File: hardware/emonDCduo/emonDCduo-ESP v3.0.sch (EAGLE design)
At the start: 84 parts, among them IC1 ACS758LCB-050B-PFF-T, IC2 ACS758LCB-050B-PFF-T, IC3 LM358D, P1 B4B-PH-K, Y1 32Khz

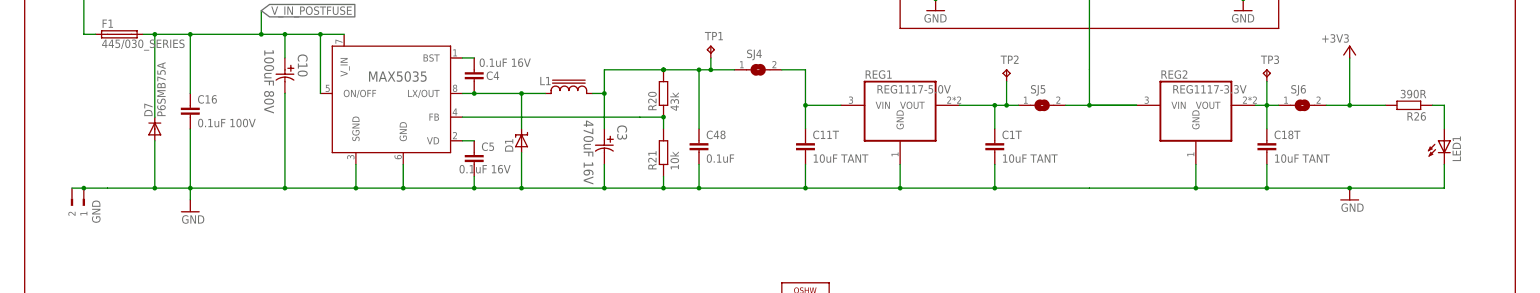
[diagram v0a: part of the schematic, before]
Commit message: starting v3.0 and ASC770 breakout
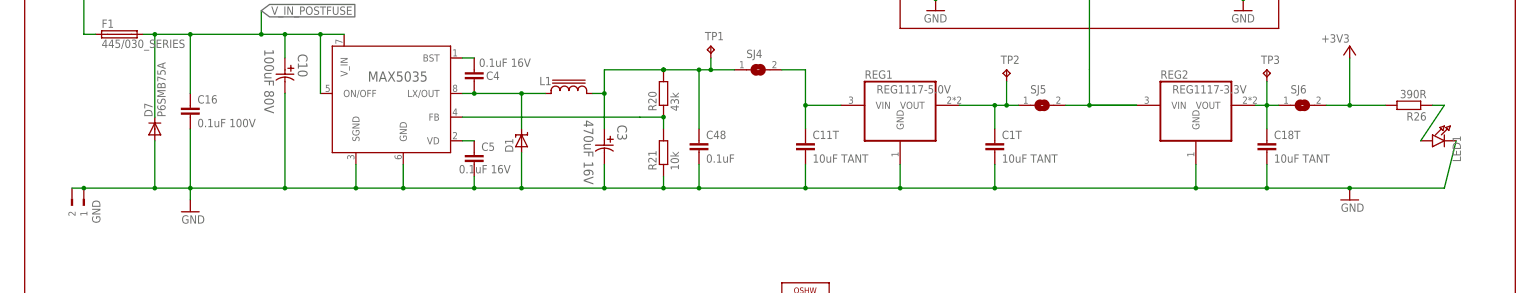
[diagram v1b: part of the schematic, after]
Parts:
- LED1: device led:LEDCHIP-LED0805 -> microbuilder:LED1206
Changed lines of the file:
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@@
 <part name="F1" library="LITTELFUSE 455:030 SERIES" deviceset="445/030_SERIES" device=""/>
 <part name="R26" library="rcl" library_urn="urn:adsk.eagle:library:334" deviceset="R-EU_" device="R0603" package3d_urn="urn:adsk.eagle:package:23555/2" value="390R"/>
-<part name="LED1" library="led" library_urn="urn:adsk.eagle:library:259" deviceset="LED" device="CHIP-LED0805" package3d_urn="urn:adsk.eagle:package:15818/2"/>
+<part name="LED1" library="microbuilder" deviceset="LED" device="1206"/>
 <part name="SJ2" library="jumper-con_db" deviceset="SJ-CON" device="CON"/>
 <part name="SJ3" library="jumper-con_db" deviceset="SJ-CON" device="CON"/>
@@
 <wire x1="30.48" y1="226.06" x2="50.8" y2="226.06" width="0.1524" layer="91"/>
 <wire x1="50.8" y1="226.06" x2="71.12" y2="226.06" width="0.1524" layer="91"/>
-<wire x1="71.12" y1="226.06" x2="91.44" y2="226.06" width="0.1524" layer="91"/>
-<wire x1="91.44" y1="226.06" x2="114.3" y2="226.06" width="0.1524" layer="91"/>
+<wire x1="71.12" y1="226.06" x2="114.3" y2="226.06" width="0.1524" layer="91"/>
 <wire x1="129.54" y1="226.06" x2="114.3" y2="226.06" width="0.1524" layer="91"/>
 <junction x="129.54" y="226.06"/>
@@
 <wire x1="-101.6" y1="226.06" x2="-109.22" y2="226.06" width="0.1524" layer="91"/>
 <pinref part="GND" gate="G$1" pin="1"/>
-<wire x1="-109.22" y1="226.06" x2="-119.38" y2="226.06" width="0.1524" layer="91"/>
-<wire x1="-119.38" y1="226.06" x2="-124.46" y2="226.06" width="0.1524" layer="91"/>
+<wire x1="-109.22" y1="226.06" x2="-124.46" y2="226.06" width="0.1524" layer="91"/>
 <wire x1="-124.46" y1="226.06" x2="-127" y2="226.06" width="0.1524" layer="91"/>
 <junction x="-124.46" y="226.06"/>
 <pinref part="GND" gate="G$1" pin="2"/>
 <pinref part="LED1" gate="G$1" pin="C"/>
-<wire x1="167.64" y1="231.14" x2="167.64" y2="226.06" width="0.1524" layer="91"/>
+<wire x1="170.18" y1="236.22" x2="167.64" y2="226.06" width="0.1524" layer="91"/>
 <wire x1="167.64" y1="226.06" x2="147.32" y2="226.06" width="0.1524" layer="91"/>
 <wire x1="-12.7" y1="226.06" x2="0" y2="226.06" width="0.1524" layer="91"/>
@@
 <pinref part="LED1" gate="G$1" pin="A"/>
 <wire x1="165.1" y1="243.84" x2="167.64" y2="243.84" width="0.1524" layer="91"/>
-<wire x1="167.64" y1="243.84" x2="167.64" y2="238.76" width="0.1524" layer="91"/>
-</segment>
-</net>
+<wire x1="167.64" y1="243.84" x2="162.56" y2="236.22" width="0.1524" layer="91"/>
+</segment>
+</net>

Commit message: commit v3.0
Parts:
- removed C10: 100uF 80V, Panasonic-EEE-EEV-EEF-ECQ:EEV-FK1K101Q-CASE-H13
- removed C16: 0.1uF 100V, rcl:C-EUC0603
- removed C2: 100nF, rcl:C-EUC0603
- removed C3: 470uF 16V, Panasonic-EEEFK_EEEFP:EEE-FK1C471P-CASE-F
- removed C4, C5: 0.1uF 16V, rcl:C-EUC0603
- removed C48, C7, C9: 0.1uF, rcl:C-EUC0603
- removed D1: MBRS1100T3G, diodes:MBRS1100T3G
- removed IC1, IC2: ACS758LCB-050B-PFF-T, allegro:ACS758LCB-050B-PFF-T
- removed IC3: LM358D, linear:LM358D
- removed J1: (no value), SparkFun-Connectors:CONN_02
- removed L1: SRR1208, inductor-bourns:SRR1208
- removed R11: 5.23k, rcl:R-EU_0204/7
- removed R20: 43k, rcl@1:R-EU_R0603
- removed R21: 10k, rcl@1:R-EU_R0603
- removed REG0: MAX5035, MAX5035:MAX5035
- removed SJ7: (no value), jumper:SJ
- removed UART_RFM: UART_RFM, JeeLabs:MA06-1
- added 7.62_BARRIER: GMSTBA2, con-phoenix-762:GMSTBA2
- added C12, C13, C14, C15, C17, C18, C20: 1nF, rcl:C-EUC0603
- added C19: 0.1uF, rcl:C-EUC0603
- added C23, C24, C25: 0.1uF 100V, rcl:C-EUC0603
- added D2, D3, D4, D5: P6SMB75A, diode:DIODE-DO214AA
- added EBW_A, EBW_B: EBW_SERIES_15.2MM, EBW series SHUNT:EBW_SERIES_15.2MM
- added F2, F3, F4, F5: (no value), fuse:TR5
- added LM258: (no value), microbuilder:LM358
- added MCP3208: MCP3208-BI/SL, MCP3208:MCP3208-BI/SL
- added MOUNT_10.16_A, MOUNT_10.16_B: MOLEX_39970-003, 10.16mm terminal block:MOLEX_39970-003
- added MOUNT_7.62_A, MOUNT_7.62_B: GMSTBV2, con-phoenix-762:GMSTBV2
- added PWR, REF_SEL_A, REF_SEL_B: 455-1750-1-ND, SparkFun-Connectors:CONN_03
- added R4: 1K, rcl:R-EU_R0603
- added R8: 2K, rcl:R-EU_R0603
- added SHUNTMON-A, SHUNTMON-B: LMP8481, lmp8481b:LMP8481-H
- added SJ1: (no value), jumper-con_db:SJ-CONCON
- added TP4, TP5, TP6, TP7: TPPAD1-13Y, testpad:TPPAD1-13Y
- C11: value 0.1uF 100V -> 1nF; MPN C1608X7S2A104K080AB -> (none)
- C11T, C18T, C1T: device rcl:C-EUC0603 -> rcl7:CPOL-EUC0603POL
- C7T: device rcl@1:C-EUC0603 -> rcl7:CPOL-EUC0603POL
- R1, R14: value 1.5M 3.5kV -> 1M 100V; device rcl7:R-EU_0411/15 -> rcl:R-EU_R0603
- R10: value 16.56k -> 174R; device rcl:R-EU_0204/7 -> rcl7:R-EU_0207/10
- R13: value 5.23k -> 10k; device rcl7:R-EU_R0603 -> rcl7:R-EU_0207/10
- R15, R2: value 100K -> 56K
- R26: value 390R -> 174R
- R5: value 517.77k -> 5.6k; device rcl7:R-EU_R0603 -> rcl7:R-EU_0207/10
- renumbered BOOT to ESPBOOT
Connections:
- net N$30 renamed RESET
- removed net BST: C4.1, REG0.BST
- removed net CH6: J5.2
- removed net LX: C4.2, D1.C, L1.1, REG0.LX/OUT
- removed net N$10: C7T.1, PCF8523.VDD, R9.1
- removed net N$20: UART_RFM.5
- removed net N$3: IC2.IP+, MH4.MOUNT
- removed net N$301: C2.2, UART_RFM.1
- removed net N$4: J1.2
- removed net N$6: J1.1
- removed net N$9: IC3B.+IN, R1.1, R2.2
- removed net PRE_6.5V: C3.1, C48.1, L1.2, R20.2, SJ4.1, TP1.TP
- removed net VD: C5.1, REG0.VD
- new net GPIO12A: MCP3208.DOUT, R4.1
- new net LOAD-NEG-A_T: C1.1, C23.2, D2.C, F2.2, SHUNTMON-A.RSN
- new net LOAD-NEG-B: EBW_A.P$2, F4.1, MH4.MOUNT, MOUNT_10.16_B.P$1, MOUNT_7.62_A-2.1
- new net LOAD-NEG-B_T: C24.2, C8.1, D4.C, F4.2, SHUNTMON-B.RSN
- new net REF_A_INPUT: REF_SEL_A.2, SHUNTMON-A.REFA, SHUNTMON-A.REFB
- new net REF_B_INPUT: REF_SEL_B.2, SHUNTMON-B.REFA, SHUNTMON-B.REFB
- new net SOURCE-POS-A_T: C1.2, C25.1, D3.C, F3.2, R14.2, SHUNTMON-A.RSP
- new net SOURCE-POS-B_T: C6.1, C8.2, D5.C, F5.2, R1.2, SHUNTMON-B.RSP
- new net VDD_PCF: C7T.+, PCF8523.VDD, R9.1
- new net VSENSE_B: LM258G$2.+IN, R1.1, R2.2
- net +3V3: now also C18.1, MCP3208.CH6
- net +5V: now also C19.1, LM258G$1.V+, MCP3208.VDD, MCP3208.VREF, R13.2, SHUNTMON-A.VCC, SHUNTMON-B.VCC; no longer C1.1, C8.1, IC1.VCC, IC2.VCC, R10.2, R5.1, UART_RFM.4
- net 3.3V_PRE: now also C18T.+; no longer C18T.1
- net 5V_PRE: now also 7.62_BARRIER-2.1, C1T.+; no longer C1T.1
- net 6.5V: now also C11T.+; no longer C11T.1
- net ADCSHUNT_A: now also C17.1, MCP3208.CH0, SHUNTMON-A.VOUT; no longer C6.1, IC1.VOUT
- net ADCSHUNT_B: now also C12.1, MCP3208.CH2, SHUNTMON-B.VOUT; no longer C11.1, IC2.VOUT
- net BI_REF: now also C14.1, MCP3208.CH4, R13.1, R5.2, REF_SEL_A.3, REF_SEL_B.3; no longer C7.1, R10.1, R11.2
- net CH7: now also C20.1, MCP3208.CH7
- net D0/RX: no longer UART_RFM.2
- net D1/TX: no longer UART_RFM.3
- net GND: now also 7.62_BARRIER-1.1, C11T.-, C18T.-, C19.2, C1T.-, C23.1, C24.1, C25.2, C7T.-, D2.A, D3.A, D4.A, D5.A, J5.2, LM258G$1.V-, MCP3208.AGND, MCP3208.DGND, R10.1, R8.2, SHUNTMON-A.GND, SHUNTMON-B.GND, TP6.TP, TP7.TP; no longer C1.2, C10.2, C11.2, C11T.2, C16.2, C18T.2, C1T.2, C3.2, C48.2, C5.2, C7.2, C7T.2, C8.2, C9.2, D1.A, IC1.GND, IC2.GND, R11.1, R13.2, R21.1, REG0.GND, REG0.SGND, UART_RFM.6
- net GPIO12: now also R4.2, R8.1
- net GPIO13: now also MCP3208.DIN
- net GPIO14: now also MCP3208.CLK
- net GPIO16: now also SJ1.2; no longer SJ7.1
- net GPIO2: now also MCP3208.!CS
- net LOAD-NEG-A: now also EBW_B.P$2, F2.1, MOUNT_10.16_A.P$1, MOUNT_7.62_B-2.1; no longer IC1.IP+
- net N$1: now also SJ4.1, TP1.TP, TP5.TP; no longer R20.1, R21.2, REG0.FB
- net RST: now also SJ1.1; no longer SJ7.2
- net SOURCE-POS-A: now also EBW_B.P$1, F3.1, MOUNT_10.16_A.P$2, MOUNT_7.62_B-1.1, PWR.3; no longer IC1.IP-, R14.2
- net SOURCE-POS-B: now also EBW_A.P$1, F5.1, MOUNT_10.16_B.P$2, MOUNT_7.62_A-1.1, PWR.1; no longer IC2.IP-, R1.2
- net UNI_REF: now also C15.1, MCP3208.CH5, R10.2, R5.1, REF_SEL_A.1, REF_SEL_B.1; no longer C9.1, R13.1, R5.2
- net VSENSE_A: now also LM258G$1.+IN; no longer IC3A.+IN
- net VSENSE_A_BUFF: now also C11.1, LM258G$1.-IN, LM258G$1.OUT, MCP3208.CH1; no longer IC3A.-IN, IC3A.OUT
- net VSENSE_B_BUFF: now also C13.1, LM258G$2.-IN, LM258G$2.OUT, MCP3208.CH3; no longer IC3B.-IN, IC3B.OUT
- net V_IN_POSTFUSE: now also TP4.TP; no longer C10.1, C16.1, REG0.ON/OFF, REG0.V_IN
- net V_IN_PREFUSE: now also PWR.2
- net _RESET: no longer C2.1
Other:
- note added: "50mV MIN output desirable"
- note added: "MCP3208"
- note added: "SPI LCD DISPLAY"
- note added: "designed by Daniel Bates November 2018"
- note added: "emonDC v3.0 use of ESP module inspired by Heatpumpmonitor project. RTC layout taken from IoTaWatt."
- note removed: "I2C LCD DISPLAY"
- note removed: "STM32"
- note removed: "designed by Daniel Bates July 2018"
- note removed: "emonDC v2.4 based on emonTx and Heatpumpmonitor"
- moved on the sheet: C1, C11, C6, C8, J5, LED1, MH1, MH2, MH3, MH4, R10, R13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

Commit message: commit v3.1
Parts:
- removed C21, C22: 100nF, rcl:C-EUC0603
- removed C23, C24: 0.1uF 100V, rcl:C-EUC0603
- removed MOUNT_7.62_A, MOUNT_7.62_B: GMSTBV2, con-phoenix-762:GMSTBV2
- removed R18: 2k, rcl:R-EU_R0603
- removed R26: 174R, rcl:R-EU_R0603
- removed R27, R28: 10K, rcl:R-EU_R0603
- removed SJ3: (no value), jumper-con_db:SJ-CONCON
- added C10, C9: 1nF, rcl:C-EUC0603
- added C2, C4, C5, C7: 0.1uF 100V, rcl:C-EUC0603
- added R11, R20, R21: 10K, rcl:R-EU_R0603
- added R22: 1K, rcl@1:R-EU_R0603
- added TP10, TP11, TP8, TP9: TPPAD1-13Y, testpad:TPPAD1-13Y
- C17, C18: value 1nF -> 0.1uF
- C33T: value 10uF -> 10uF TANT
- LED1: value (none) -> PWR_ON
- R10: value 174R -> 2K; device rcl7:R-EU_0207/10 -> rcl:R-EU_R0603; MPN (none) -> MCWR06X5901FTL
- R13: value 10k -> 10K; device rcl7:R-EU_0207/10 -> rcl:R-EU_R0603
- R14: value 1M 100V -> 1k; MPN MCWR06X1003FTL -> (none)
- R15: value 56K -> 2k; MPN MCWR06X5901FTL -> (none)
- R17: value 1k -> 10K
- R3: value 10K -> 1M 100V; MPN (none) -> MCWR06X1003FTL
- R4: value 1K -> 56K
- R5: value 5.6k -> 174R; device rcl7:R-EU_0207/10 -> rcl:R-EU_R0603
- R6: value 10K -> 10k; device rcl:R-EU_R0603 -> rcl7:R-EU_0207/10
- R7: value 10K -> 5.6k; device rcl:R-EU_R0603 -> rcl7:R-EU_0207/10
- R8: value 2K -> 174R; device rcl:R-EU_R0603 -> rcl7:R-EU_0207/10; MPN MCWR06X5901FTL -> (none)
- R9: device rcl@1:R-EU_R0603 -> rcl:R-EU_R0603; MPN (none) -> MCWR06X5901FTL
- SJ2: device jumper-con_db:SJ-CONCON -> jumper:SJ
- UART: value UART_ESP -> UART
- renumbered C11T to C30T, C18T to C32T, C1T to C31T, C20 to C16, C25 to C3, C7T to C33T, D7 to D1, R19 to R16, UART_ESP to UART
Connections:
- removed net N$24: R9.2, SJ2.2
- removed net VCC_ESP: C22.2, ESP-12.VCC, R12.2, R16.2, R6.2, R7.2, SJ3.1
- new net VDD_RTC_POSTJUMPER: R20.1, R21.1, R22.2, SJ2.2
- net +3V3: now also C15.1, C17.2, ESP-12.VCC, R12.2, R13.2, R16.2, R17.2, R5.2; no longer C18.1, R26.2, R27.1, R28.1, SJ3.2
- net +5V: now also R6.2; no longer R13.2
- net ADCSHUNT_A: now also C9.1; no longer C17.1
- net ADCSHUNT_B: now also C11.1; no longer C12.1
- net BI_REF: now also C13.1, R6.1, R7.2; no longer C14.1, R13.1, R5.2
- net CH_PD: now also C18.1, R17.1; no longer C21.1, R7.1
- net ESPRX: now also R14.2, R15.1; no longer R17.2, R18.1
- net GND: now also C1.2, C17.1, C4.2, C7.2, C8.2, R10.2, R11.2, R15.2, R4.1, R8.1; no longer C22.1, C23.1, C24.1, R10.1, R15.1, R18.2, R3.2, R8.2
- net GPIO0: now also R13.1; no longer R12.1
- net GPIO12: now also R10.1, R9.2; no longer R4.2, R8.1
- net GPIO12A: now also R9.1; no longer R4.1
- net GPIO15: now also R11.1; no longer R3.1
- net GPIO2: now also R12.1; no longer R6.1
- net LOAD-NEG-A: now also TP11.TP; no longer MOUNT_7.62_B-2.1
- net LOAD-NEG-A_T: now also C2.1; no longer C23.2
- net LOAD-NEG-B: now also TP9.TP; no longer MOUNT_7.62_A-2.1
- net LOAD-NEG-B_T: now also C4.1, C5.1; no longer C24.2, C8.1
- net N$36: now also R14.1; no longer R17.1
- net N$5: now also R5.1; no longer R26.1
- net REF_A_INPUT: now also C7.1
- net REF_B_INPUT: now also C8.1
- net RESET: now also C18.2; no longer C21.2
- net SCL: no longer R27.2
- net SDA: no longer R28.2
- net SOURCE-POS-A: now also TP10.TP; no longer MOUNT_7.62_B-1.1
- net SOURCE-POS-A_T: now also C2.2, R1.2; no longer C1.2, R14.2
- net SOURCE-POS-B: now also TP8.TP; no longer MOUNT_7.62_A-1.1
- net SOURCE-POS-B_T: now also C5.2, R3.2; no longer C8.2, R1.2
- net UNI_REF: now also C14.1, R7.1, R8.2; no longer C15.1, R10.2, R5.1
- net VDD_PCF: now also R22.1; no longer R9.1
- net VSENSE_A: now also R1.1, R2.2; no longer R14.1, R15.2
- net VSENSE_A_BUFF: now also C10.1; no longer C11.1
- net VSENSE_B: now also R3.1, R4.2; no longer R1.1, R2.2
- net VSENSE_B_BUFF: now also C12.1; no longer C13.1
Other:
- note added: "ESP-12E/S/F"
- note removed: "ESP-12S"
- moved on the sheet: C1, C11, C12, C13, C14, C15, C17, C18, C8, R1, R10, R12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
